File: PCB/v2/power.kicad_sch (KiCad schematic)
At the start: 35 parts, among them J1 XT60PW-M, U2 BTS7002-1EPP, U3 AP63200WU-7, U4 AP7361C-33E

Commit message: pcb v2: lcsc numbers, availability checked
Claude-Session: https://claude.ai/code/session_015oqRiQH5gUcw5a6jvR5Zdk
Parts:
- C1, C2: LCSC (none) -> C2983550; MPN (none) -> GVZ1H107M0810CNVC; Manufacturer (none) -> HRK
- C10, C7, C8: LCSC (none) -> C14663; MPN (none) -> CC0603KRX7R9BB104; Manufacturer (none) -> YAGEO
- C11, C12, C13: LCSC (none) -> C45783; MPN (none) -> CL21A226MAQNNNE; Manufacturer (none) -> Samsung Electro-Mechanics
- C14, C15: LCSC (none) -> C15850; MPN (none) -> CL21A106KAYNNNE; Manufacturer (none) -> Samsung Electro-Mechanics
- C3, C4, C5, C6, C9: LCSC (none) -> C2918502; MPN (none) -> CS3225X7R106K500NRL; Manufacturer (none) -> SAMWHA
- D1: LCSC (none) -> C284071; MPN SMDJ18A -> 5.0SMDJ18A; Manufacturer Littelfuse -> DOWO
- D2: LCSC (none) -> C77328; Manufacturer Nexperia -> JSCJ
- D3, D4: LCSC (none) -> C8678
- D5: LCSC (none) -> C965807; MPN (none) -> XL-1608UBC-04; Manufacturer (none) -> XINGLIGHT
- J1: LCSC (none) -> C98732
- L1: LCSC (none) -> C341066; MPN (none) -> YNR6045-6R8M; Manufacturer (none) -> YJYCOIN
- R1, R2, R4, R8: LCSC (none) -> C25804; MPN (none) -> 0603WAF1002T5E; Manufacturer (none) -> UNI-ROYAL
- R10, R6: LCSC (none) -> C21190; MPN (none) -> 0603WAF1001T5E; Manufacturer (none) -> UNI-ROYAL
- R3: LCSC (none) -> C2933240; MPN (none) -> FRC0603F5762TS; Manufacturer (none) -> FOJAN
- R5: LCSC (none) -> C23179; MPN (none) -> 0603WAF4700T5E; Manufacturer (none) -> UNI-ROYAL
- R7: LCSC (none) -> C25819; MPN (none) -> 0603WAF4702T5E; Manufacturer (none) -> UNI-ROYAL
- R9: LCSC (none) -> C25803; MPN (none) -> 0603WAF1003T5E; Manufacturer (none) -> UNI-ROYAL
- U2: LCSC (none) -> C534824
- U3: LCSC (none) -> C2071868
- U4: LCSC (none) -> C500795

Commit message: pcb v2: bts7002 lcsc fix, buck note
Claude-Session: https://claude.ai/code/session_015oqRiQH5gUcw5a6jvR5Zdk
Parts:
- U2: LCSC C534824 -> C2680407; MPN BTS7002-1EPP -> BTS70021EPPXUMA1
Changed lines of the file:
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@@
       )
     )
-    (property "LCSC" "C534824"
+    (property "LCSC" "C2680407"
       (at 210.82 25.4 0)
       (hide yes)
@@
       )
     )
-    (property "MPN" "BTS7002-1EPP"
+    (property "MPN" "BTS70021EPPXUMA1"
       (at 210.82 25.4 0)
       (hide yes)

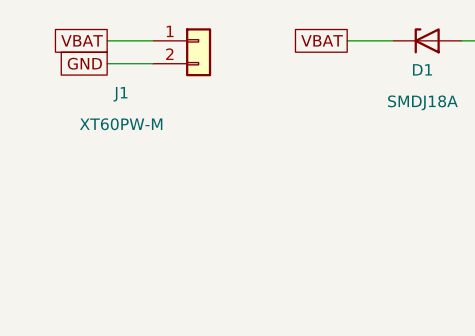
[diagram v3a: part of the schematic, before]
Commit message: pcb v2: xt60 pin 2 is +, not pin 1
Claude-Session: https://claude.ai/code/session_015oqRiQH5gUcw5a6jvR5Zdk
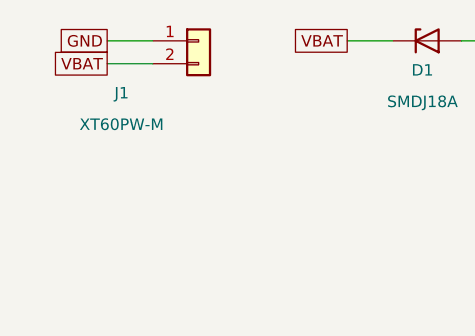
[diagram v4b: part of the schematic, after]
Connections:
- net GND: now also J1.1 (Pin_1); no longer J1.2 (Pin_2)
- net VBAT: now also J1.2 (Pin_2); no longer J1.1 (Pin_1)
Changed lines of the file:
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@@
     )
   )
-  (global_label "VBAT"
+  (global_label "GND"
     (shape passive)
     (at 20.32 12.7 180)
@@
     )
   )
-  (global_label "GND"
+  (global_label "VBAT"
     (shape passive)
     (at 20.32 15.24 180)

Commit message: pcb v2: link footprints to their symbols, widen the 12v arm, honest readmes
parity warnings 216 -> 18 (only the NC-pin net_conflicts left): footprints get
the library nickname, the sheet path and MPN/Manufacturer, and H1..H4 finally
have symbols. in2 12v arm now reaches U2's OUT pads - the band above them was
F.Cu only, 13.9 A, and the test only ever cut it at y=21. gerber dates fixed
inside the zip so a re-export is byte-identical, netlist source path made
relative, render-routed.svg dropped

Claude-Session: https://claude.ai/code/session_015oqRiQH5gUcw5a6jvR5Zdk
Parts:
- added H1, H2, H3, H4: M3, MountingHole:MountingHole_3.2mm_M3, symbol Mechanical:MountingHole
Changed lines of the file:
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@@
-      )
-    )
-    (property "LCSC" ""
-      (at 27.94 129.54 0)
-      (hide yes)
-      (effects
-        (font
-          (size 1.27 1.27)
-        )
-      )
-    )
-    (property "MPN" ""
-      (at 27.94 129.54 0)
-      (hide yes)
-      (effects
-        (font
-          (size 1.27 1.27)
-        )
-      )
-    )
-    (property "Manufacturer" ""
-      (at 27.94 129.54 0)
-      (hide yes)
-      (effects
-        (font
-          (size 1.27 1.27)
-        )
       )
     )
@@
       )
     )
-    (property "LCSC" ""
-      (at 43.18 129.54 0)
-      (hide yes)
-      (effects
-        (font
-          (size 1.27 1.27)
-        )
-      )
-    )
-    (property "MPN" ""
-      (at 43.18 129.54 0)
-      (hide yes)
-      (effects
-        (font
-          (size 1.27 1.27)
-        )
-      )
-    )
-    (property "Manufacturer" ""
-      (at 43.18 129.54 0)
-      (hide yes)
-      (effects
-        (font
-          (size 1.27 1.27)
-        )
-      )
-    )
     (pin "1"
     )
@@
       )
     )
-    (property "LCSC" ""
-      (at 60.96 129.54 0)
-      (hide yes)
-      (effects
-        (font
-          (size 1.27 1.27)
-        )
-      )
-    )
-    (property "MPN" ""
-      (at 60.96 129.54 0)
-      (hide yes)
-      (effects
-        (font
-          (size 1.27 1.27)
-        )
-      )
-    )
-    (property "Manufacturer" ""
-      (at 60.96 129.54 0)
-      (hide yes)
-      (effects
-        (font
-          (size 1.27 1.27)
-        )
-      )
-    )
     (pin "1"
     )
@@
       )
     )
-    (property "LCSC" ""
-      (at 76.2 129.54 0)
-      (hide yes)
-      (effects
-        (font
-          (size 1.27 1.27)
-        )
-      )
-    )
-    (property "MPN" ""
-      (at 76.2 129.54 0)
-      (hide yes)
-      (effects
-        (font
-          (size 1.27 1.27)
-        )
-      )
-    )
-    (property "Manufacturer" ""
-      (at 76.2 129.54 0)
-      (hide yes)
-      (effects
-        (font
-          (size 1.27 1.27)
-        )
-      )
-    )
     (pin "1"
     )
@@
       )
     )
-    (property "LCSC" ""
-      (at 91.44 129.54 0)
-      (hide yes)
-      (effects
-        (font
-          (size 1.27 1.27)
-        )
-      )
-    )
-    (property "MPN" ""
-      (at 91.44 129.54 0)
-      (hide yes)
-      (effects
-        (font
-          (size 1.27 1.27)
-        )
-      )
-    )
-    (property "Manufacturer" ""
-      (at 91.44 129.54 0)
-      (hide yes)
-      (effects
-        (font
-          (size 1.27 1.27)
-        )
-      )
-    )
     (pin "1"
     )
@@
         )
       )
+    )
+  )
+  (symbol
+    (lib_id "Mechanical:MountingHole")
+    (at 104.14 127.0 0)
+    (unit 1)
+    (body_style 1)
+    (exclude_from_sim no)
+    (in_bom no)
+    (on_board yes)
+    (in_pos_files no)
+    (dnp no)
+    (property "Reference" "H1"
+      (at 104.14 130.27 0)
+      (effects
+        (font
+          (size 1.27 1.27)
+        )
+      )
+    )
+    (property "Value" "M3"
+      (at 104.14 133.77 0)
+      (effects
+        (font
+          (size 1.27 1.27)
+        )
+      )
+    )
+    (property "Footprint" "MountingHole:MountingHole_3.2mm_M3"
+      (at 104.14 127.0 0)
+      (hide yes)
+      (effects
+        (font
+          (size 1.27 1.27)
+        )
+      )
+    )
+    (property "Datasheet" ""
+      (at 104.14 127.0 0)
+      (hide yes)
+      (effects
+        (font
+          (size 1.27 1.27)
+        )
+      )
+    )
+    (property "Description" ""
+      (at 104.14 127.0 0)
+      (hide yes)
+      (effects
+        (font
+          (size 1.27 1.27)
+        )
+      )
+    )
+    (instances
+      (project "driftanalyser-v2"
+        (path "/0d6f1c2a-0000-4000-8000-000000000001/0d6f1c2a-0000-4000-8000-000000000010"
+          (reference "H1")
+          (unit 1)
+        )
+      )
+    )
+  )
+  (symbol
+    (lib_id "Mechanical:MountingHole")
+    (at 114.3 127.0 0)
+    (unit 1)
+    (body_style 1)
+    (exclude_from_sim no)
+    (in_bom no)
+    (on_board yes)
+    (in_pos_files no)
+    (dnp no)
+    (property "Reference" "H2"
+      (at 114.3 130.27 0)
+      (effects
+        (font
+          (size 1.27 1.27)
+        )
+      )
+    )
+    (property "Value" "M3"
+      (at 114.3 133.77 0)
+      (effects
+        (font
+          (size 1.27 1.27)
+        )
+      )
+    )
+    (property "Footprint" "MountingHole:MountingHole_3.2mm_M3"
+      (at 114.3 127.0 0)
+      (hide yes)
+      (effects
+        (font
+          (size 1.27 1.27)
+        )
+      )
+    )
+    (property "Datasheet" ""
+      (at 114.3 127.0 0)
+      (hide yes)
+      (effects
+        (font
+          (size 1.27 1.27)
+        )
+      )
+    )
+    (property "Description" ""
+      (at 114.3 127.0 0)
+      (hide yes)
+      (effects
+        (font
+          (size 1.27 1.27)
+        )
+      )
+    )
+    (instances
+      (project "driftanalyser-v2"
+        (path "/0d6f1c2a-0000-4000-8000-000000000001/0d6f1c2a-0000-4000-8000-000000000010"
+          (reference "H2")
+          (unit 1)
+        )
+      )
+    )
+  )
+  (symbol
+    (lib_id "Mechanical:MountingHole")
+    (at 124.46 127.0 0)
+    (unit 1)
+    (body_style 1)
+    (exclude_from_sim no)
+    (in_bom no)
+    (on_board yes)
+    (in_pos_files no)
+    (dnp no)
+    (property "Reference" "H3"
+      (at 124.46 130.27 0)
+      (effects
+        (font
+          (size 1.27 1.27)
+        )
+      )
+    )
+    (property "Value" "M3"
+      (at 124.46 133.77 0)
+      (effects
+        (font
+          (size 1.27 1.27)
+        )
+      )
+    )
+    (property "Footprint" "MountingHole:MountingHole_3.2mm_M3"
+      (at 124.46 127.0 0)
+      (hide yes)
+      (effects
+        (font
+          (size 1.27 1.27)
+        )
+      )
+    )
+    (property "Datasheet" ""
+      (at 124.46 127.0 0)
+      (hide yes)
+      (effects
+        (font
+          (size 1.27 1.27)
+        )
+      )
+    )
+    (property "Description" ""
+      (at 124.46 127.0 0)
+      (hide yes)
+      (effects
+        (font
+          (size 1.27 1.27)
+        )
+      )
+    )
+    (instances
+      (project "driftanalyser-v2"
+        (path "/0d6f1c2a-0000-4000-8000-000000000001/0d6f1c2a-0000-4000-8000-000000000010"
+          (reference "H3")
+          (unit 1)
+        )
+      )
+    )
+  )
+  (symbol
+    (lib_id "Mechanical:MountingHole")
+    (at 134.62 127.0 0)
+    (unit 1)
+    (body_style 1)
+    (exclude_from_sim no)
+    (in_bom no)
+    (on_board yes)
+    (in_pos_files no)
+    (dnp no)
+    (property "Reference" "H4"
+      (at 134.62 130.27 0)
+      (effects
+        (font
+          (size 1.27 1.27)
+        )
+      )
+    )
+    (property "Value" "M3"
+      (at 134.62 133.77 0)
+      (effects
+        (font
+          (size 1.27 1.27)
+        )
+      )
+    )
+    (property "Footprint" "MountingHole:MountingHole_3.2mm_M3"
+      (at 134.62 127.0 0)
+      (hide yes)
+      (effects
+        (font
+          (size 1.27 1.27)
+        )
+      )
+    )
+    (property "Datasheet" ""
+      (at 134.62 127.0 0)
+      (hide yes)
+      (effects
+        (font
+          (size 1.27 1.27)
+        )
+      )
+    )
+    (property "Description" ""
+      (at 134.62 127.0 0)
+      (hide yes)
+      (effects
+        (font
+          (size 1.27 1.27)
+        )
+      )
+    )
+    (instances
+      (project "driftanalyser-v2"
+        (path "/0d6f1c2a-0000-4000-8000-000000000001/0d6f1c2a-0000-4000-8000-000000000010"
+          (reference "H4")
+          (unit 1)
+        )
+      )

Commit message: pcb v2: c1/c2 are 50v not 35v
GVZ1H107M0810CNVC (C2983550) is a 50V part, the 35V label was a typo. same part, nothing to reorder

Claude-Session: https://claude.ai/code/session_011XKWp7yoGtzw88WQygPeEA
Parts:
- C1, C2: value 100uF 35V -> 100uF 50V
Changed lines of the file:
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@@
       )
     )
-    (property "Value" "100uF 35V"
+    (property "Value" "100uF 50V"
       (at 86.36 52.02 0)
       (effects
@@
       )
     )
-    (property "Value" "100uF 35V"
+    (property "Value" "100uF 50V"
       (at 101.6 52.02 0)
       (effects
